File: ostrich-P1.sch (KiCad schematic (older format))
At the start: 102 parts

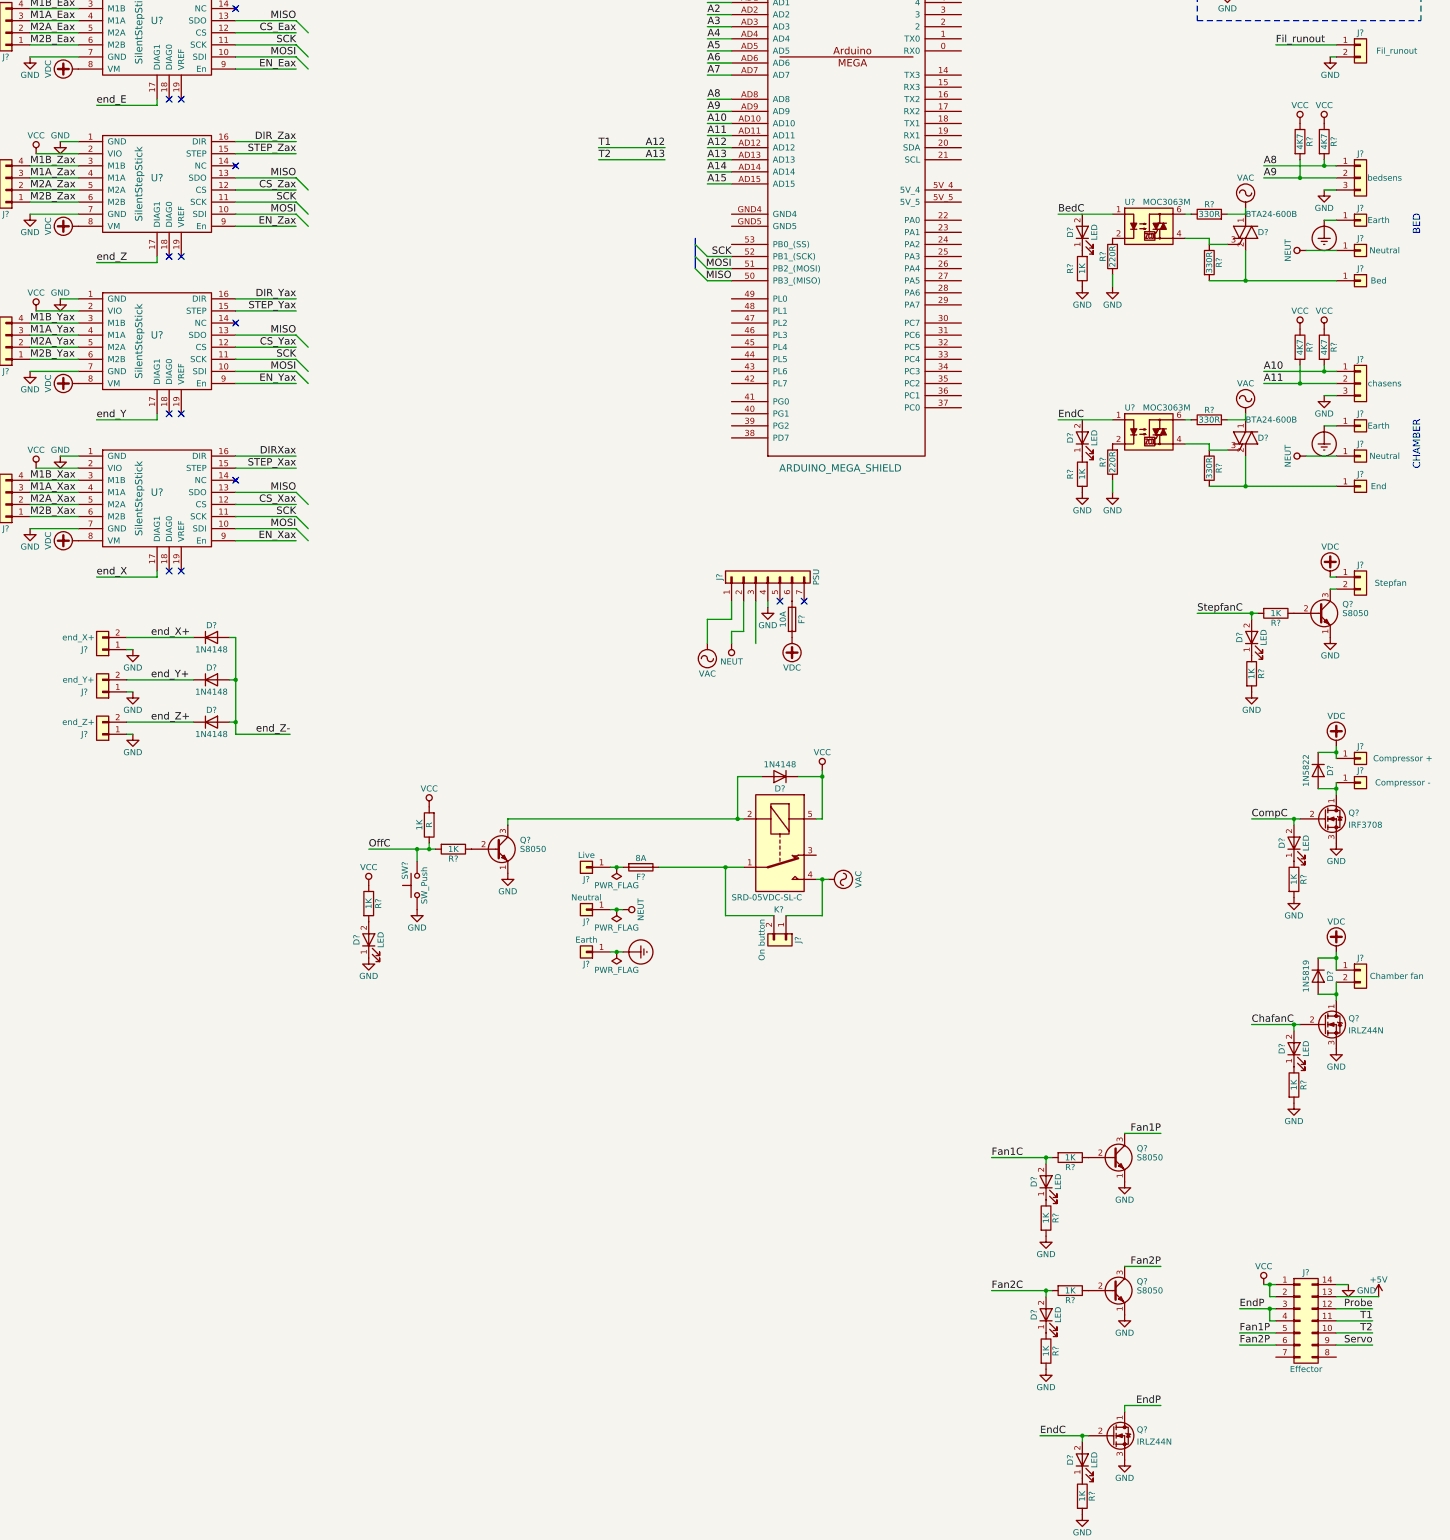
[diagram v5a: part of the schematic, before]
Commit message: Added thermistor comparators and smoke detector header.
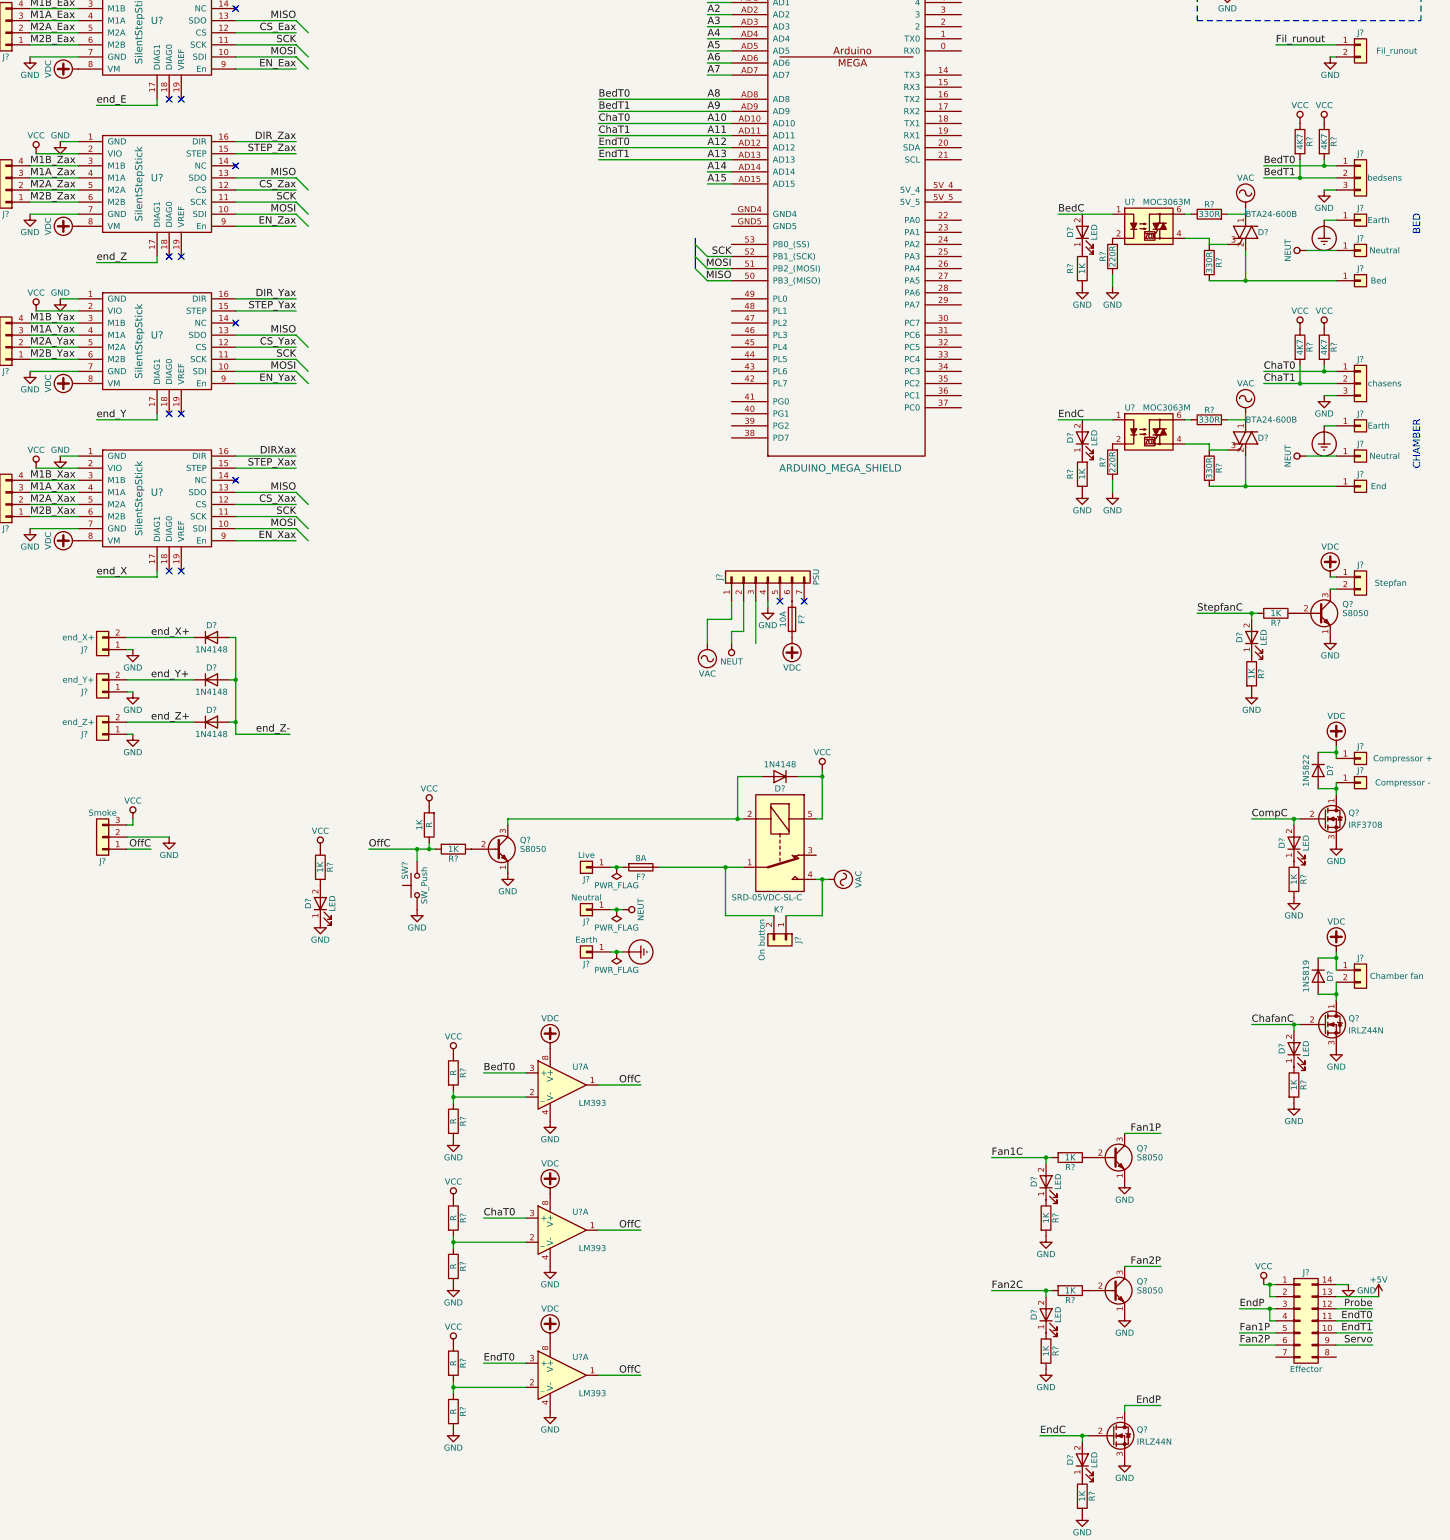
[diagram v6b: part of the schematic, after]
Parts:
- added J?: Smoke, symbol Conn_01x03
- added R? (x6): R, symbol R
- added U? (x3): LM393, symbol LM393
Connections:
- net A10: now also U?.3 (+)
- net A12: now also U?.3 (+)
- net A8: now also U?.3 (+)
- net GND: now also J?.2 (Pin_2), R?.2, R?.2, R?.2, U?.4 (V-), U?.4 (V-), U?.4 (V-)
- net OffC: now also J?.1 (Pin_1), U?.1, U?.1, U?.1
- net VCC: now also J?.3 (Pin_3), R?.1, R?.1, R?.1
- net VDC: now also U?.8 (V+), U?.8 (V+), U?.8 (V+)
- new net: R?.1, R?.2, U?.2 (_) (x3)
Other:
- moved on the sheet: D?, R?
